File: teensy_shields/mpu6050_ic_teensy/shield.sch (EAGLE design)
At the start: 6 parts

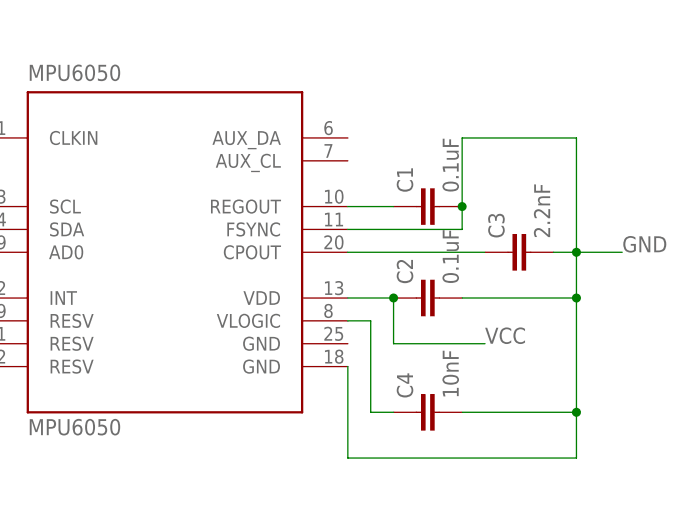
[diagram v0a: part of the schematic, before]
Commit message: Switched files
Corrected file directories
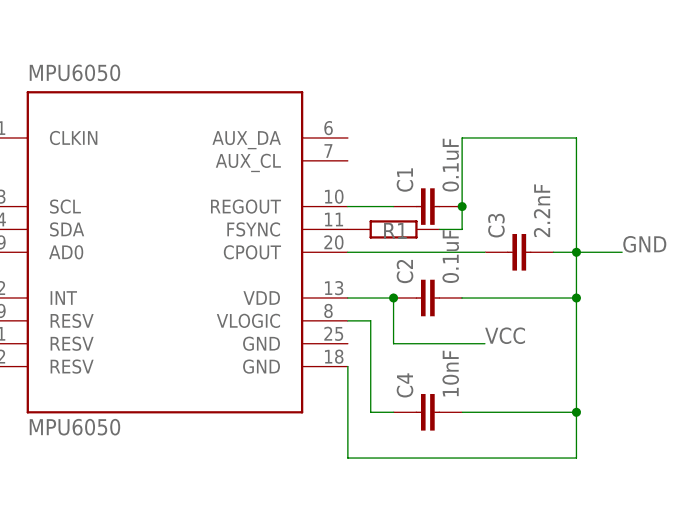
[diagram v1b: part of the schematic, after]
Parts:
- added R1: (no value), eagle-ltspice:RR0603
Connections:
- new net N$4: MPU6050G$1.FSYNC, R1.1
- net GND: now also R1.2; no longer MPU6050G$1.FSYNC
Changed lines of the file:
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@@
 <part name="C1" library="SparkFun-Capacitors" deviceset="0.1UF" device="-0603-25V-(+80/-20%)" value="0.1uF"/>
 <part name="C4" library="SparkFun-Capacitors" deviceset="10NF" device="-0603-50V-10%" value="10nF"/>
+<part name="R1" library="eagle-ltspice" library_urn="urn:adsk.eagle:library:217" deviceset="R" device="R0603" package3d_urn="urn:adsk.eagle:package:13302/1"/>
 </parts>
 <sheets>
@@
 <attribute name="NAME" x="152.019" y="42.164" size="1.778" layer="95" font="vector" rot="R90"/>
 <attribute name="VALUE" x="157.099" y="42.164" size="1.778" layer="96" font="vector" rot="R90"/>
+</instance>
+<instance part="R1" gate="G$1" x="149.86" y="60.96">
+<attribute name="NAME" x="148.59" y="59.9186" size="1.778" layer="95"/>
+<attribute name="VALUE" x="146.05" y="57.658" size="1.778" layer="96"/>
 </instance>
 </instances>
@@
 <junction x="170.18" y="58.42"/>
 <wire x1="170.18" y1="58.42" x2="170.18" y2="71.12" width="0.1524" layer="91"/>
-<pinref part="MPU6050" gate="G$1" pin="FSYNC"/>
-<wire x1="144.78" y1="60.96" x2="157.48" y2="60.96" width="0.1524" layer="91"/>
 <wire x1="157.48" y1="60.96" x2="157.48" y2="63.5" width="0.1524" layer="91"/>
 <wire x1="157.48" y1="63.5" x2="157.48" y2="71.12" width="0.1524" layer="91"/>
@@
 <wire x1="170.18" y1="35.56" x2="170.18" y2="40.64" width="0.1524" layer="91"/>
 <junction x="170.18" y="40.64"/>
+<wire x1="154.94" y1="60.96" x2="157.48" y2="60.96" width="0.1524" layer="91"/>
+<pinref part="R1" gate="G$1" pin="2"/>
 </segment>
 <segment>
@@
 </segment>
 </net>
+<net name="N$4" class="0">
+<segment>
+<pinref part="MPU6050" gate="G$1" pin="FSYNC"/>
+<pinref part="R1" gate="G$1" pin="1"/>
+</segment>
+</net>
 </nets>
 </sheet>
@@
 </schematic>
 </drawing>
+<compatibility>
+<note version="8.2" severity="warning">
+Since Version 8.2, EAGLE supports online libraries. The ids
+of those online libraries will not be understood (or retained)
+with this version.
+</note>
+<note version="8.3" severity="warning">
+Since Version 8.3, EAGLE supports URNs for individual library
+assets (packages, symbols, and devices). The URNs of those assets
+will not be understood (or retained) with this version.
+</note>
+<note version="8.3" severity="warning">
+Since Version 8.3, EAGLE supports the association of 3D packages
+with devices in libraries, schematics, and board files. Those 3D
+packages will not be understood (or retained) with this version.
+</note>
+</compatibility>
 </eagle>

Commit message: clean up
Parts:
- added U$1: DEV, Custom_old (1):DEV
- C1, C2: device SparkFun-Capacitors:0.1UF-0603-25V-(+80/-20%) -> SparkFun-Passives:CAP0603-CAP
- C3: device SparkFun-Capacitors:2.2NF/2200PF-0603-50V-10% -> SparkFun-Passives:CAP0603-CAP
- C4: device SparkFun-Capacitors:10NF-0603-50V-10% -> SparkFun-Passives:CAP0603-CAP
- R1: value (none) -> 10k; device eagle-ltspice:RR0603 -> SparkFun-Passives:RESISTOR0603-RES
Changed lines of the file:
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@@
 <?xml version="1.0" encoding="utf-8"?>
 <!DOCTYPE eagle SYSTEM "eagle.dtd">
-<eagle version="9.2.0">
+<eagle version="9.1.1">
 <drawing>
 <settings>
@@
 <layer number="230" name="230bmp" color="7" fill="1" visible="no" active="no"/>
 <layer number="231" name="231bmp" color="7" fill="1" visible="no" active="no"/>
+<layer number="232" name="Eagle3D_PG2" color="7" fill="1" visible="no" active="no"/>
+<layer number="233" name="Eagle3D_PG3" color="7" fill="1" visible="no" active="no"/>
 <layer number="248" name="Housing" color="7" fill="1" visible="no" active="no"/>
 <layer number="249" name="Edge" color="7" fill="1" visible="no" active="no"/>
@@
 </classes>
 <parts>
-<part name="TEENSY" library="Teensy" deviceset="TEENSY_3.1-3.2_ALL_PINS" device=""/>
+<part name="TEENSY" library="Teensy" deviceset="TEENSY_3.1-3.2_ALL_PINS" device="" value=""/>
 <part name="MPU6050" library="invensense" deviceset="MPU6050" device=""/>
-<part name="C3" library="SparkFun-Capacitors" deviceset="2.2NF/2200PF" device="-0603-50V-10%" value="2.2nF"/>
-<part name="C2" library="SparkFun-Capacitors" deviceset="0.1UF" device="-0603-25V-(+80/-20%)" value="0.1uF"/>
-<part name="C1" library="SparkFun-Capacitors" deviceset="0.1UF" device="-0603-25V-(+80/-20%)" value="0.1uF"/>
-<part name="C4" library="SparkFun-Capacitors" deviceset="10NF" device="-0603-50V-10%" value="10nF"/>
-<part name="R1" library="eagle-ltspice" library_urn="urn:adsk.eagle:library:217" deviceset="R" device="R0603" package3d_urn="urn:adsk.eagle:package:13302/1"/>
+<part name="C3" library="SparkFun-Passives" deviceset="CAP" device="0603-CAP" value="2.2nF"/>
+<part name="C2" library="SparkFun-Passives" deviceset="CAP" device="0603-CAP" value="0.1uF"/>
+<part name="C1" library="SparkFun-Passives" deviceset="CAP" device="0603-CAP" value="0.1uF"/>
+<part name="C4" library="SparkFun-Passives" deviceset="CAP" device="0603-CAP" value="10nF"/>
+<part name="R1" library="SparkFun-Passives" deviceset="RESISTOR" device="0603-RES" value="10k"/>
+<part name="U$1" library="Custom_old (1)" deviceset="DEV" device=""/>
 </parts>
 <sheets>
@@
 <attribute name="NAME" x="109.22" y="77.47" size="1.778" layer="95" font="vector" ratio="10"/>
 </instance>
-<instance part="C3" gate="G$1" x="165.1" y="58.42" rot="R90">
-<attribute name="NAME" x="162.179" y="59.944" size="1.778" layer="95" font="vector" rot="R90"/>
-<attribute name="VALUE" x="167.259" y="59.944" size="1.778" layer="96" font="vector" rot="R90"/>
-</instance>
-<instance part="C2" gate="G$1" x="154.94" y="53.34" rot="R90">
-<attribute name="NAME" x="152.019" y="54.864" size="1.778" layer="95" font="vector" rot="R90"/>
-<attribute name="VALUE" x="157.099" y="54.864" size="1.778" layer="96" font="vector" rot="R90"/>
-</instance>
-<instance part="C1" gate="G$1" x="154.94" y="63.5" rot="R90">
-<attribute name="NAME" x="152.019" y="65.024" size="1.778" layer="95" font="vector" rot="R90"/>
-<attribute name="VALUE" x="157.099" y="65.024" size="1.778" layer="96" font="vector" rot="R90"/>
-</instance>
-<instance part="C4" gate="G$1" x="154.94" y="40.64" rot="R90">
-<attribute name="NAME" x="152.019" y="42.164" size="1.778" layer="95" font="vector" rot="R90"/>
-<attribute name="VALUE" x="157.099" y="42.164" size="1.778" layer="96" font="vector" rot="R90"/>
-</instance>
+<instance part="C3" gate="G$1" x="165.1" y="58.42" rot="R90"/>
+<instance part="C2" gate="G$1" x="154.94" y="53.34" rot="R90"/>
+<instance part="C1" gate="G$1" x="154.94" y="63.5" rot="R90"/>
+<instance part="C4" gate="G$1" x="154.94" y="40.64" rot="R90"/>
 <instance part="R1" gate="G$1" x="149.86" y="60.96">
-<attribute name="NAME" x="148.59" y="59.9186" size="1.778" layer="95"/>
 <attribute name="VALUE" x="146.05" y="57.658" size="1.778" layer="96"/>
 </instance>
+<instance part="U$1" gate="G$1" x="137.16" y="88.9"/>
 </instances>
 <busses>
@@
 </schematic>
 </drawing>
-<compatibility>
-<note version="8.2" severity="warning">
-Since Version 8.2, EAGLE supports online libraries. The ids
-of those online libraries will not be understood (or retained)
-with this version.
-</note>
-<note version="8.3" severity="warning">
-Since Version 8.3, EAGLE supports URNs for individual library
-assets (packages, symbols, and devices). The URNs of those assets
-will not be understood (or retained) with this version.
-</note>
-<note version="8.3" severity="warning">
-Since Version 8.3, EAGLE supports the association of 3D packages
-with devices in libraries, schematics, and board files. Those 3D
-packages will not be understood (or retained) with this version.
-</note>
-</compatibility>
 </eagle>
